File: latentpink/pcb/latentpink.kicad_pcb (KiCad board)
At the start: 8 copper layers, 145 x 134 mm, 244 parts, among them J1 CONN_SFP_HOST, J10 XILINX_JTAG, J13 CONN_01X05, J14 CONN_01X03, J2 SFP_CAGE, J3 RJ45, J4 RJ45, J5 BEL_FUSE_0826-1G1T-23-F, J6 BARREL_JACK, J7 RJ45, J8 08263-2X6R-54-F, J9 XILINX_JTAG, M1 960-27-12-D-AB-0, M2 960-23-23-F-AB-0, M3 SCREWHOLE, M4 SCREWHOLE, M5 SCREWHOLE, M6 SCREWHOLE, U1 VSC8512, U10 MYMGK1R812ERSR, U11 MYMGK00504ERSR, U12 STM32L031-QFN32, U13 MYMGK00504ERSR, U14 MYMGK00504ERSR, U15 MYMGK00504ERSR, U16 NCP45521IMNTWG-H, U17 NCP45521IMNTWG-H, U18 LP2996AMRE, U2 XC7K160T-2FBG484C, U3 CY7C2245KV18-450BZXI, U4 STM32H735-UFBGA176-25, U5 DP83867, U6 DP83867, U7 BEL_FUSE_S558-5999-M8-F, U8 BEL_FUSE_S558-5999-M8-F, U9 KSZ9031RN

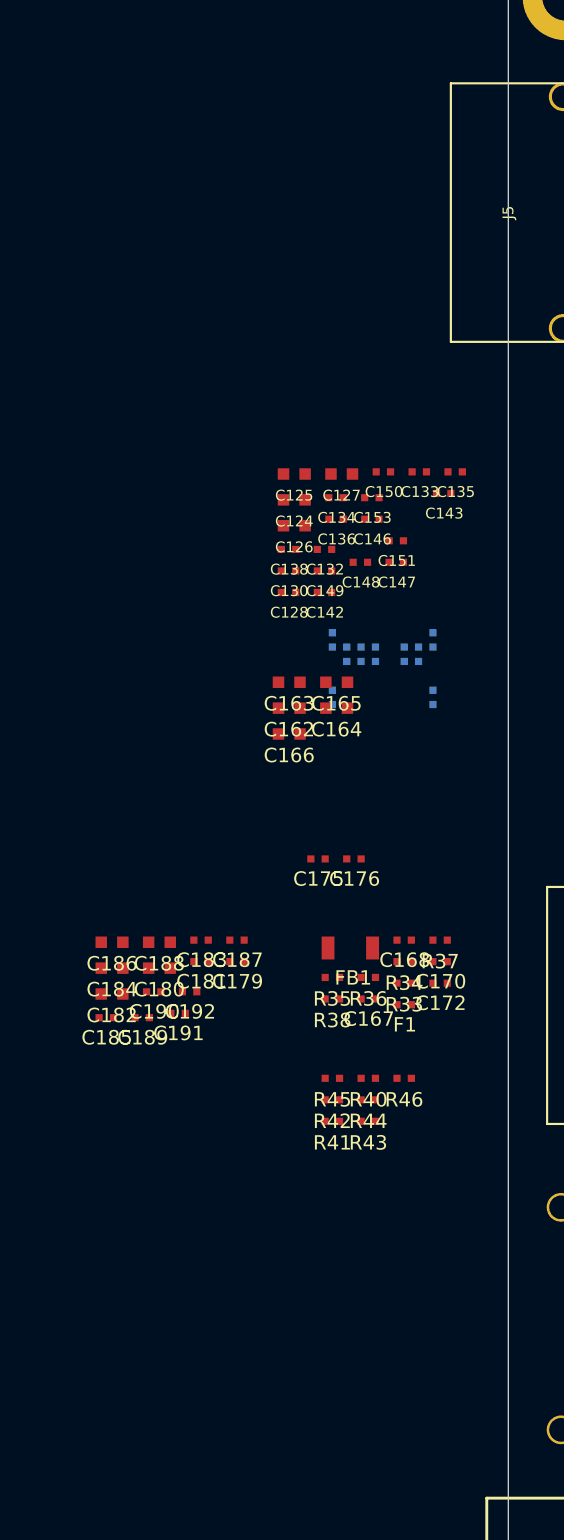
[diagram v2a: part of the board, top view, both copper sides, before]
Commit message: Initial version of RGMII PHY schematic
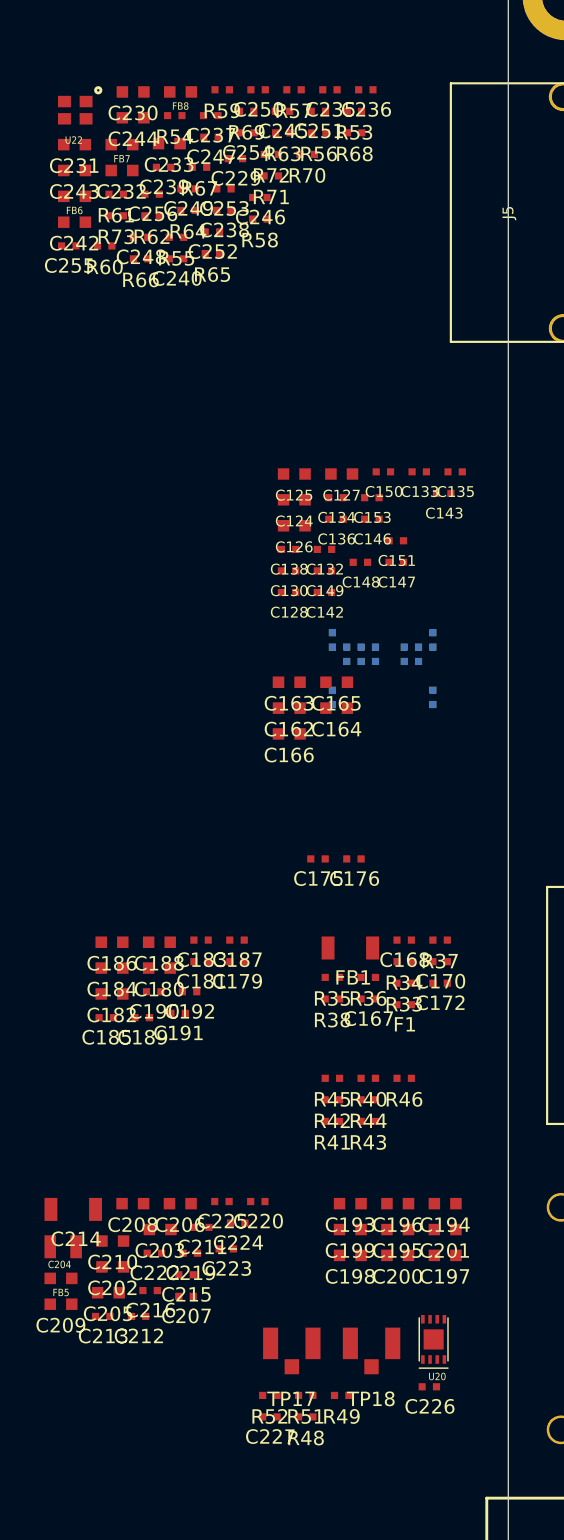
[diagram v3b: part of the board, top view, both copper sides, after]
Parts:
- added C193: 4.7 uF, azonenberg_pcb:EIA_0603_CAP_NOSILK, F.Cu at (26.0, 111.0)
- added C194: 4.7 uF, azonenberg_pcb:EIA_0603_CAP_NOSILK, F.Cu at (32.6, 111.0)
- added C195: 4.7 uF, azonenberg_pcb:EIA_0603_CAP_NOSILK, F.Cu at (29.3, 112.8)
- added C196: 4.7 uF, azonenberg_pcb:EIA_0603_CAP_NOSILK, F.Cu at (29.3, 111.0)
- added C197: 4.7 uF, azonenberg_pcb:EIA_0603_CAP_NOSILK, F.Cu at (32.6, 114.6)
- added C198: 4.7 uF, azonenberg_pcb:EIA_0603_CAP_NOSILK, F.Cu at (26.0, 114.6)
- added C199: 4.7 uF, azonenberg_pcb:EIA_0603_CAP_NOSILK, F.Cu at (26.0, 112.8)
- added C200: 4.7 uF, azonenberg_pcb:EIA_0603_CAP_NOSILK, F.Cu at (29.3, 114.6)
- added C201: 4.7 uF, azonenberg_pcb:EIA_0603_CAP_NOSILK, F.Cu at (32.6, 112.8)
- added C202: 4.7 uF, azonenberg_pcb:EIA_0603_CAP_NOSILK, F.Cu at (9.46, 115.4)
- added C203: 4.7 uF, azonenberg_pcb:EIA_0603_CAP_NOSILK, F.Cu at (12.8, 112.8)
- added C204: 10 uF, azonenberg_pcb:EIA_0805_CAP_NOSILK, F.Cu at (6.01, 114.0)
- added C205: 2.2 uF, azonenberg_pcb:EIA_0603_CAP_NOSILK, F.Cu at (9.16, 117.2)
- added C206: 4.7 uF, azonenberg_pcb:EIA_0603_CAP_NOSILK, F.Cu at (14.2, 111.0)
- added C207: 0.1 uF, azonenberg_pcb:EIA_0402_CAP_NOSILK, F.Cu at (14.6, 117.5)
- added C208: 4.7 uF, azonenberg_pcb:EIA_0603_CAP_NOSILK, F.Cu at (10.9, 111.0)
- added C209: 2.2 uF, azonenberg_pcb:EIA_0603_CAP_NOSILK, F.Cu at (5.86, 118.0)
- added C210: 4.7 uF, azonenberg_pcb:EIA_0603_CAP_NOSILK, F.Cu at (9.46, 113.6)
- added C211: 0.47 uF, azonenberg_pcb:EIA_0402_CAP_NOSILK, F.Cu at (15.7, 112.7)
- added C212: 0.47 uF, azonenberg_pcb:EIA_0402_CAP_NOSILK, F.Cu at (11.3, 118.8)
- added C213: 0.47 uF, azonenberg_pcb:EIA_0402_CAP_NOSILK, F.Cu at (8.76, 118.8)
- added C214: 22 uF, azonenberg_pcb:EIA_1206_CAP_NOSILK, F.Cu at (6.71, 111.4)
- added C215: 0.47 uF, azonenberg_pcb:EIA_0402_CAP_NOSILK, F.Cu at (14.6, 116.0)
- added C216: 0.47 uF, azonenberg_pcb:EIA_0402_CAP_NOSILK, F.Cu at (12.1, 117.0)
- added C219: 0.47 uF, azonenberg_pcb:EIA_0402_CAP_NOSILK, F.Cu at (14.9, 114.5)
- added C220: 0.47 uF, azonenberg_pcb:EIA_0402_CAP_NOSILK, F.Cu at (19.6, 110.8)
- added C222: 0.47 uF, azonenberg_pcb:EIA_0402_CAP_NOSILK, F.Cu at (12.4, 114.5)
- added C223: 0.47 uF, azonenberg_pcb:EIA_0402_CAP_NOSILK, F.Cu at (17.4, 114.2)
- added C224: 0.47 uF, azonenberg_pcb:EIA_0402_CAP_NOSILK, F.Cu at (18.2, 112.3)
- added C225: 0.47 uF, azonenberg_pcb:EIA_0402_CAP_NOSILK, F.Cu at (17.1, 110.8)
- added C226: 0.1 uF, azonenberg_pcb:EIA_0402_CAP_NOSILK, F.Cu at (31.5, 123.8)
- added C227: 0.47 uF, azonenberg_pcb:EIA_0402_CAP_NOSILK, F.Cu at (20.4, 125.8)
- added C229: 0.1 uF, azonenberg_pcb:EIA_0402_CAP_NOSILK, F.Cu at (18.0, 38.2)
- added C230: 4.7 uF, azonenberg_pcb:EIA_0603_CAP_NOSILK, F.Cu at (10.9, 33.6)
- added C231: 4.7 uF, azonenberg_pcb:EIA_0603_CAP_NOSILK, F.Cu at (6.80, 37.3)
- added C232: 4.7 uF, azonenberg_pcb:EIA_0603_CAP_NOSILK, F.Cu at (10.1, 39.1)
- added C233: 4.7 uF, azonenberg_pcb:EIA_0603_CAP_NOSILK, F.Cu at (13.4, 37.2)
- added C235: 0.1 uF, azonenberg_pcb:EIA_0402_CAP_NOSILK, F.Cu at (24.6, 33.5)
- added C236: 0.1 uF, azonenberg_pcb:EIA_0402_CAP_NOSILK, F.Cu at (27.1, 33.5)
- added C237: 0.1 uF, azonenberg_pcb:EIA_0402_CAP_NOSILK, F.Cu at (16.3, 35.2)
- added C238: 0.1 uF, azonenberg_pcb:EIA_0402_CAP_NOSILK, F.Cu at (17.2, 41.9)
- added C239: 0.47 uF, azonenberg_pcb:EIA_0402_CAP_NOSILK, F.Cu at (13.0, 38.9)
- added C240: 0.47 uF, azonenberg_pcb:EIA_0402_CAP_NOSILK, F.Cu at (13.9, 45.2)
- added C242: 4.7 uF, azonenberg_pcb:EIA_0603_CAP_NOSILK, F.Cu at (6.80, 42.7)
- added C243: 4.7 uF, azonenberg_pcb:EIA_0603_CAP_NOSILK, F.Cu at (6.80, 39.1)
- added C244: 4.7 uF, azonenberg_pcb:EIA_0603_CAP_NOSILK, F.Cu at (10.9, 35.4)
- added C245: 0.47 uF, azonenberg_pcb:EIA_0402_CAP_NOSILK, F.Cu at (21.3, 35.0)
- added C246: 0.47 uF, azonenberg_pcb:EIA_0402_CAP_NOSILK, F.Cu at (19.7, 41.0)
- added C247: 0.47 uF, azonenberg_pcb:EIA_0402_CAP_NOSILK, F.Cu at (16.3, 36.8)
- added C248: 0.47 uF, azonenberg_pcb:EIA_0402_CAP_NOSILK, F.Cu at (11.4, 43.7)
- added C249: 0.47 uF, azonenberg_pcb:EIA_0402_CAP_NOSILK, F.Cu at (14.7, 40.4)
- added C250: 0.47 uF, azonenberg_pcb:EIA_0402_CAP_NOSILK, F.Cu at (19.6, 33.5)
- added C251: 0.47 uF, azonenberg_pcb:EIA_0402_CAP_NOSILK, F.Cu at (23.8, 35.0)
- added C252: 0.47 uF, azonenberg_pcb:EIA_0402_CAP_NOSILK, F.Cu at (16.4, 43.4)
- added C253: 0.47 uF, azonenberg_pcb:EIA_0402_CAP_NOSILK, F.Cu at (17.2, 40.4)
- added C254: 0.47 uF, azonenberg_pcb:EIA_0402_CAP_NOSILK, F.Cu at (18.8, 36.5)
- added C255: 0.47 uF, azonenberg_pcb:EIA_0402_CAP_NOSILK, F.Cu at (6.40, 44.3)
- added C256: 0.47 uF, azonenberg_pcb:EIA_0402_CAP_NOSILK, F.Cu at (12.2, 40.7)
- added FB5: FERRITE_SMALL2, azonenberg_pcb:EIA_0603_INDUCTOR_NOSILK, F.Cu at (5.86, 116.2)
- added FB6: MI0603J601R-10, azonenberg_pcb:EIA_0603_INDUCTOR_NOSILK, F.Cu at (6.80, 40.9)
- added FB7: MI0603J601R-10, azonenberg_pcb:EIA_0603_INDUCTOR_NOSILK, F.Cu at (10.1, 37.3)
- added FB8: MI0603J601R-10, azonenberg_pcb:EIA_0603_INDUCTOR_NOSILK, F.Cu at (14.2, 33.6)
- added R48: 10K, azonenberg_pcb:EIA_0402_RES_NOSILK, F.Cu at (22.9, 125.8)
- added R49: 10K, azonenberg_pcb:EIA_0402_RES_NOSILK, F.Cu at (25.4, 124.3)
- added R51: 4.7K, azonenberg_pcb:EIA_0402_RES_NOSILK, F.Cu at (22.9, 124.3)
- added R52: 4.7K, azonenberg_pcb:EIA_0402_RES_NOSILK, F.Cu at (20.4, 124.3)
- added R53: 1M, azonenberg_pcb:EIA_0402_RES_NOSILK, F.Cu at (26.3, 35.0)
- added R54: 470, azonenberg_pcb:EIA_0402_RES_NOSILK, F.Cu at (13.8, 35.2)
- added R55: 470, azonenberg_pcb:EIA_0402_RES_NOSILK, F.Cu at (13.9, 43.7)
- added R56: 33, azonenberg_pcb:EIA_0402_RES_NOSILK, F.Cu at (23.8, 36.5)
- added R57: 1K, azonenberg_pcb:EIA_0402_RES_NOSILK, F.Cu at (22.1, 33.5)
- added R58: 33, azonenberg_pcb:EIA_0402_RES_NOSILK, F.Cu at (19.7, 42.5)
- added R59: 33, azonenberg_pcb:EIA_0402_RES_NOSILK, F.Cu at (17.1, 33.5)
- added R60: 33, azonenberg_pcb:EIA_0402_RES_NOSILK, F.Cu at (8.90, 44.3)
- added R61: 33, azonenberg_pcb:EIA_0402_RES_NOSILK, F.Cu at (9.70, 40.7)
- added R62: 33, azonenberg_pcb:EIA_0402_RES_NOSILK, F.Cu at (12.2, 42.2)
- added R63: 33, azonenberg_pcb:EIA_0402_RES_NOSILK, F.Cu at (21.3, 36.5)
- added R64: 12.1K 1%, azonenberg_pcb:EIA_0402_RES_NOSILK, F.Cu at (14.7, 41.9)
- added R65: 1K, azonenberg_pcb:EIA_0402_RES_NOSILK, F.Cu at (16.4, 44.9)
- added R66: 10K, azonenberg_pcb:EIA_0402_RES_NOSILK, F.Cu at (11.4, 45.2)
- added R67: 10K, azonenberg_pcb:EIA_0402_RES_NOSILK, F.Cu at (15.5, 38.9)
- added R68: 10K, azonenberg_pcb:EIA_0402_RES_NOSILK, F.Cu at (26.3, 36.5)
- added R69: 10K, azonenberg_pcb:EIA_0402_RES_NOSILK, F.Cu at (18.8, 35.0)
- added R70: 10K, azonenberg_pcb:EIA_0402_RES_NOSILK, F.Cu at (23.0, 38.0)
- added R71: 10K, azonenberg_pcb:EIA_0402_RES_NOSILK, F.Cu at (20.5, 39.5)
- added R72: 10K, azonenberg_pcb:EIA_0402_RES_NOSILK, F.Cu at (20.5, 38.0)
- added R73: 1K, azonenberg_pcb:EIA_0402_RES_NOSILK, F.Cu at (9.70, 42.2)
- added TP17: U.FL, azonenberg_pcb:CONN_U.FL_TE_1909763-1, F.Cu at (21.9, 120.8)
- added TP18: U.FL, azonenberg_pcb:CONN_U.FL_TE_1909763-1, F.Cu at (27.5, 120.8)
- added U20: AT24MAC402, azonenberg_pcb:DFN_8_0.5MM_2x3MM_TALL, F.Cu at (31.8, 120.5)
- added U22: ECS-2016MVQ-250-CN, azonenberg_pcb:OSCILLATOR_2.0x1.6, F.Cu at (6.85, 34.9)
- J5: value BEL_FUSE_0826-1G1T-23-F -> 0826-1G1T-23-F
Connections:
- J10 pad 10: unconnected-(J10-Pad10) -> /Management/MCU_JTAG_TDI
- J10 pad 11: unconnected-(J10-Pad11) -> /GND
- J10 pad 2: unconnected-(J10-Pad2) -> /3V3
- J10 pad 3: unconnected-(J10-Pad3) -> /GND
- J10 pad 4: unconnected-(J10-Pad4) -> /Management/MCU_JTAG_TMS
- J10 pad 5: unconnected-(J10-Pad5) -> /GND
- J10 pad 6: unconnected-(J10-Pad6) -> /Management/MCU_JTAG_TCK
- J10 pad 7: unconnected-(J10-Pad7) -> /GND
- J10 pad 8: unconnected-(J10-Pad8) -> /Management/MCU_JTAG_TDO
- J10 pad 9: unconnected-(J10-Pad9) -> /GND
- J5 pad 1: unconnected-(J5-Pad1) -> Net-(J5-Pad1)
- J5 pad 10: unconnected-(J5-Pad10) -> /Management/RGMII PHY/ETH_A_N
- J5 pad 11: unconnected-(J5-Pad11) -> /Management/RGMII PHY/ETH_A_P
- J5 pad 12: unconnected-(J5-Pad12) -> Net-(J5-Pad12)
- J5 pad 13: unconnected-(J5-Pad13) -> /GND
- J5 pad 14: unconnected-(J5-Pad14) -> Net-(J5-Pad14)
- J5 pad 15: unconnected-(J5-Pad15) -> /GND
- J5 pad 16: unconnected-(J5-Pad16) -> Net-(J5-Pad16)
- J5 pad 17: unconnected-(J5-Pad17) -> Net-(J5-Pad17)
- J5 pad 2: unconnected-(J5-Pad2) -> /Management/RGMII PHY/ETH_C_N
- J5 pad 3: unconnected-(J5-Pad3) -> /Management/RGMII PHY/ETH_C_P
- J5 pad 4: unconnected-(J5-Pad4) -> /Management/RGMII PHY/ETH_B_P
- J5 pad 5: unconnected-(J5-Pad5) -> /Management/RGMII PHY/ETH_B_N
- J5 pad 6: unconnected-(J5-Pad6) -> Net-(J5-Pad6)
- J5 pad 7: unconnected-(J5-Pad7) -> Net-(J5-Pad7)
- J5 pad 8: unconnected-(J5-Pad8) -> /Management/RGMII PHY/ETH_D_P
- J5 pad 9: unconnected-(J5-Pad9) -> /Management/RGMII PHY/ETH_D_N
- U12 pad 14: /Power Supply/MCU_RST_N -> /MCU_RST_N
- U12 pad 15: /Power Supply/FPGA_RST_N -> /FPGA/FPGA_RST_N
- U12 pad 16: /Power Supply/FPGA_DONE -> /FPGA/FPGA_DONE
- U12 pad 26: /Power Supply/FPGA_INIT -> /FPGA/FPGA_INIT
- U2 pad A10: unconnected-(U2-PadA10) -> /Management/MCU_QSPI_DQ3
- U2 pad A11: unconnected-(U2-PadA11) -> /Management/MCU_QSPI_DQ2
- U2 pad A8: unconnected-(U2-PadA8) -> /Management/MCU_QSPI_CLK
- U2 pad A9: unconnected-(U2-PadA9) -> /Management/MCU_IRQ
- U2 pad AA4: unconnected-(U2-PadAA4) -> /Management/RGMII PHY/ETH_LED1_N_1V8
- U2 pad AB3: unconnected-(U2-PadAB3) -> /Management/RGMII PHY/ETH_LED2_N_1V8
- U2 pad B8: unconnected-(U2-PadB8) -> /Management/MCU_QSPI_DQ1
- U2 pad C8: unconnected-(U2-PadC8) -> /Management/MCU_QSPI_DQ0
- U2 pad D10: unconnected-(U2-PadD10) -> /Management/ETH_LED2_P
- U2 pad E8: unconnected-(U2-PadE8) -> /Management/MCU_QSPI_CS_N
- U2 pad F14: unconnected-(U2-PadF14) -> /Management/ETH_LED1_P
- U2 pad F19: /FPGA/QDR SRAM/QDR_A1 -> /FPGA/QDR SRAM/FPGA_FLASH_DQ3
- U2 pad G18: /FPGA/QDR SRAM/QDR_A0 -> /FPGA/QDR SRAM/FPGA_FLASH_DQ2
- U2 pad H18: /FPGA/QDR SRAM/QDR_RPS_N -> /FPGA/QDR SRAM/FPGA_FLASH_DQ0
- U2 pad H19: /FPGA/QDR SRAM/QDR_QVLD -> /FPGA/QDR SRAM/FPGA_FLASH_DQ1
- U2 pad K18: /FPGA/QDR SRAM/QDR_A2 -> Net-(U2-PadK18)
- U2 pad K22: unconnected-(U2-PadK22) -> /FPGA/QDR SRAM/QDR_A8
- U2 pad K4: unconnected-(U2-PadK4) -> /Management/RGMII PHY/DCI_VRN_34
- U2 pad L16: /FPGA/QDR SRAM/QDR_A8 -> /FPGA/QDR SRAM/FPGA_FLASH_CS_N
- U2 pad L21: unconnected-(U2-PadL21) -> /FPGA/QDR SRAM/QDR_A1
- U2 pad L3: unconnected-(U2-PadL3) -> /Management/RGMII PHY/ETH_LED1_N_1V8
- U2 pad L4: unconnected-(U2-PadL4) -> /Management/RGMII PHY/RGMII_TXD3
- U2 pad L5: unconnected-(U2-PadL5) -> /Management/RGMII PHY/RGMII_TXD2
- U2 pad M20: unconnected-(U2-PadM20) -> /FPGA/QDR SRAM/QDR_A0
- U2 pad M21: unconnected-(U2-PadM21) -> /FPGA/QDR SRAM/QDR_QVLD
- U2 pad M3: unconnected-(U2-PadM3) -> /Management/RGMII PHY/ETH_LED2_N_1V8
- U2 pad M5: unconnected-(U2-PadM5) -> /Management/RGMII PHY/ETH_RST_N
- U2 pad N2: unconnected-(U2-PadN2) -> /Management/RGMII PHY/RGMII_TXD1
- U2 pad N20: unconnected-(U2-PadN20) -> /FPGA/QDR SRAM/QDR_RPS_N
- U2 pad N3: unconnected-(U2-PadN3) -> /Management/RGMII PHY/RGMII_TXD0
- U2 pad N4: unconnected-(U2-PadN4) -> /Management/RGMII PHY/ETH_RXD3
- U2 pad P1: unconnected-(U2-PadP1) -> /Management/RGMII PHY/ETH_MDC
- U2 pad P2: unconnected-(U2-PadP2) -> /Management/RGMII PHY/RGMII_TX_CLK
- U2 pad P4: unconnected-(U2-PadP4) -> /Management/RGMII PHY/ETH_RXD0
- U2 pad R1: unconnected-(U2-PadR1) -> /Management/RGMII PHY/ETH_MDIO
- U2 pad R18: unconnected-(U2-PadR18) -> /FPGA/QDR SRAM/QDR_A2
- U2 pad R2: unconnected-(U2-PadR2) -> /Management/RGMII PHY/RGMII_TX_EN
- U2 pad R3: unconnected-(U2-PadR3) -> /Management/RGMII PHY/CLK_125_P
- U2 pad R4: unconnected-(U2-PadR4) -> /Management/RGMII PHY/ETH_RX_DV
- U2 pad T1: unconnected-(U2-PadT1) -> /Management/RGMII PHY/ETH_RXD2
- U2 pad T3: unconnected-(U2-PadT3) -> /Management/RGMII PHY/CLK_125_N
- U2 pad T4: unconnected-(U2-PadT4) -> /Management/RGMII PHY/ETH_RX_CLK
- U2 pad U1: unconnected-(U2-PadU1) -> /Management/RGMII PHY/ETH_RXD1
- U2 pad V5: unconnected-(U2-PadV5) -> /Management/RGMII PHY/DCI_VRP_34
- U4 pad A11: unconnected-(U4-PadA11) -> /Management/MCU_JTAG_TDI
- U4 pad A12: unconnected-(U4-PadA12) -> /Management/MCU_JTAG_TCK
- U4 pad A13: unconnected-(U4-PadA13) -> /Management/MCU_VSMPS
- U4 pad A14: unconnected-(U4-PadA14) -> /Management/VCORE
- U4 pad A3: unconnected-(U4-PadA3) -> /Management/MCU_VSMPS
- U4 pad A4: unconnected-(U4-PadA4) -> /Management/VCORE
- U4 pad A6: unconnected-(U4-PadA6) -> Net-(U4-PadA6)
- U4 pad B13: unconnected-(U4-PadB13) -> /Management/MCU_JTAG_TMS
- U4 pad B15: unconnected-(U4-PadB15) -> /Management/MCU_UART_TX
- U4 pad C15: unconnected-(U4-PadC15) -> /Management/MCU_UART_RX
- U4 pad C5: unconnected-(U4-PadC5) -> /Management/MCU_BOOT0
- U4 pad D11: unconnected-(U4-PadD11) -> /3V3
- U4 pad D4: unconnected-(U4-PadD4) -> /3V3
- U4 pad D5: unconnected-(U4-PadD5) -> /3V3
- U4 pad E12: unconnected-(U4-PadE12) -> /3V3
- U4 pad E15: unconnected-(U4-PadE15) -> /3V3
- U4 pad E2: unconnected-(U4-PadE2) -> /3V3
- U4 pad E4: unconnected-(U4-PadE4) -> /3V3
- U4 pad F1: unconnected-(U4-PadF1) -> /Management/VLXSMPS
- U4 pad F13: unconnected-(U4-PadF13) -> /3V3
- U4 pad G1: unconnected-(U4-PadG1) -> /3V3
- U4 pad G2: unconnected-(U4-PadG2) -> /Management/VSMPS
- U4 pad G4: unconnected-(U4-PadG4) -> /3V3
- U4 pad H12: unconnected-(U4-PadH12) -> /3V3
- U4 pad K4: unconnected-(U4-PadK4) -> /3V3
- U4 pad L1: unconnected-(U4-PadL1) -> /MCU_RST_N
- U4 pad L12: unconnected-(U4-PadL12) -> /3V3
- U4 pad L4: unconnected-(U4-PadL4) -> /GND
- U4 pad M1: unconnected-(U4-PadM1) -> /Management/MCU_QSPI_DQ2
- U4 pad M3: unconnected-(U4-PadM3) -> /3V3
- U4 pad M4: unconnected-(U4-PadM4) -> /Management/MCU_VDDA
- U4 pad M5: unconnected-(U4-PadM5) -> /3V3
- U4 pad M9: unconnected-(U4-PadM9) -> /3V3
- U4 pad P1: unconnected-(U4-PadP1) -> /Management/MCU_IRQ
- U4 pad P2: unconnected-(U4-PadP2) -> /Management/MCU_QSPI_DQ3
- U4 pad P7: unconnected-(U4-PadP7) -> /Management/MCU_QSPI_CLK
- U4 pad R12: unconnected-(U4-PadR12) -> /Management/MCU_QSPI_CS_N
- U4 pad R13: unconnected-(U4-PadR13) -> /Management/VCORE
- U4 pad R14: unconnected-(U4-PadR14) -> /Management/MCU_VSMPS
- U4 pad R2: unconnected-(U4-PadR2) -> /Management/MCU_QSPI_DQ0
- U4 pad R8: unconnected-(U4-PadR8) -> /Management/MCU_QSPI_DQ1
- U9 pad 1: unconnected-(U9-Pad1) -> /Management/RGMII PHY/A2V5
- U9 pad 10: unconnected-(U9-Pad10) -> /Management/RGMII PHY/ETH_D_P
- U9 pad 11: unconnected-(U9-Pad11) -> /Management/RGMII PHY/ETH_D_N
- U9 pad 12: unconnected-(U9-Pad12) -> /Management/RGMII PHY/A2V5
- U9 pad 13: unconnected-(U9-Pad13) -> /GND
- U9 pad 14: unconnected-(U9-Pad14) -> /1V2
- U9 pad 15: unconnected-(U9-Pad15) -> /Management/RGMII PHY/ETH_LED2_N_1V8
- U9 pad 16: unconnected-(U9-Pad16) -> /1V8_IO
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
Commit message: Continued work on QSGMII subsystem
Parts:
- added C257: 0.47 uF, azonenberg_pcb:EIA_0402_CAP_NOSILK, F.Cu at (252.5, 59.8)
- added C258: 0.1 uF, azonenberg_pcb:EIA_0402_CAP_NOSILK, F.Cu at (104.5, 78.8)
- added C259: 0.1 uF, azonenberg_pcb:EIA_0402_CAP_NOSILK, F.Cu at (102.0, 80.2)
- added C260: 0.1 uF, azonenberg_pcb:EIA_0402_CAP_NOSILK, F.Cu at (102.0, 78.8)
- added C261: 0.1 uF, azonenberg_pcb:EIA_0402_CAP_NOSILK, F.Cu at (104.5, 80.2)
- added C264: 0.47 uF, azonenberg_pcb:EIA_0402_CAP_NOSILK, F.Cu at (228.0, 71.8)
- added C266: 0.47 uF, azonenberg_pcb:EIA_0402_CAP_NOSILK, F.Cu at (220.5, 69.7)
- added C267: 4.7 uF, azonenberg_pcb:EIA_0603_CAP_NOSILK, F.Cu at (220.9, 63.5)
- added C268: 0.47 uF, azonenberg_pcb:EIA_0402_CAP_NOSILK, F.Cu at (228.0, 68.8)
- added C269: 0.47 uF, azonenberg_pcb:EIA_0402_CAP_NOSILK, F.Cu at (234.6, 59.8)
- added C270: 0.47 uF, azonenberg_pcb:EIA_0402_CAP_NOSILK, F.Cu at (233.0, 67.2)
- added C271: 0.47 uF, azonenberg_pcb:EIA_0402_CAP_NOSILK, F.Cu at (239.6, 59.8)
- added C272: 0.47 uF, azonenberg_pcb:EIA_0402_CAP_NOSILK, F.Cu at (220.5, 66.7)
- added C273: 0.47 uF, azonenberg_pcb:EIA_0402_CAP_NOSILK, F.Cu at (236.3, 64.2)
- added C274: 0.47 uF, azonenberg_pcb:EIA_0402_CAP_NOSILK, F.Cu at (239.6, 61.2)
- added C275: 0.47 uF, azonenberg_pcb:EIA_0402_CAP_NOSILK, F.Cu at (233.8, 62.8)
- added C276: 0.47 uF, azonenberg_pcb:EIA_0402_CAP_NOSILK, F.Cu at (220.5, 68.2)
- added C277: 0.47 uF, azonenberg_pcb:EIA_0402_CAP_NOSILK, F.Cu at (230.5, 71.8)
- added C278: 0.47 uF, azonenberg_pcb:EIA_0402_CAP_NOSILK, F.Cu at (228.8, 64.2)
- added C279: 0.47 uF, azonenberg_pcb:EIA_0402_CAP_NOSILK, F.Cu at (242.1, 59.8)
- added C280: 0.47 uF, azonenberg_pcb:EIA_0402_CAP_NOSILK, F.Cu at (223.0, 66.7)
- added C281: 0.47 uF, azonenberg_pcb:EIA_0402_CAP_NOSILK, F.Cu at (228.8, 62.8)
- added C282: 0.47 uF, azonenberg_pcb:EIA_0402_CAP_NOSILK, F.Cu at (223.0, 71.2)
- added C285: 0.47 uF, azonenberg_pcb:EIA_0402_CAP_NOSILK, F.Cu at (228.0, 65.8)
- added C286: 0.47 uF, azonenberg_pcb:EIA_0402_CAP_NOSILK, F.Cu at (230.5, 68.8)
- added C287: 0.47 uF, azonenberg_pcb:EIA_0402_CAP_NOSILK, F.Cu at (235.5, 67.2)
- added C288: 0.47 uF, azonenberg_pcb:EIA_0402_CAP_NOSILK, F.Cu at (230.5, 65.8)
- added C290: 0.47 uF, azonenberg_pcb:EIA_0402_CAP_NOSILK, F.Cu at (242.1, 61.2)
- added C291: 0.47 uF, azonenberg_pcb:EIA_0402_CAP_NOSILK, F.Cu at (233.8, 64.2)
- added C292: 4.7 uF, azonenberg_pcb:EIA_0603_CAP_NOSILK, F.Cu at (224.2, 59.9)
- added C293: 4.7 uF, azonenberg_pcb:EIA_0603_CAP_NOSILK, F.Cu at (220.9, 61.7)
- added C294: 0.47 uF, azonenberg_pcb:EIA_0402_CAP_NOSILK, F.Cu at (233.0, 68.8)
- added C295: 0.47 uF, azonenberg_pcb:EIA_0402_CAP_NOSILK, F.Cu at (234.6, 61.2)
- added C296: 0.47 uF, azonenberg_pcb:EIA_0402_CAP_NOSILK, F.Cu at (223.8, 63.4)
- added C297: 0.47 uF, azonenberg_pcb:EIA_0402_CAP_NOSILK, F.Cu at (225.5, 70.8)
- added C298: 0.47 uF, azonenberg_pcb:EIA_0402_CAP_NOSILK, F.Cu at (233.0, 65.8)
- added C299: 0.47 uF, azonenberg_pcb:EIA_0402_CAP_NOSILK, F.Cu at (232.1, 59.8)
- added C300: 0.47 uF, azonenberg_pcb:EIA_0402_CAP_NOSILK, F.Cu at (225.5, 67.8)
- added C302: 0.47 uF, azonenberg_pcb:EIA_0402_CAP_NOSILK, F.Cu at (238.8, 62.8)
- added C303: 0.47 uF, azonenberg_pcb:EIA_0402_CAP_NOSILK, F.Cu at (225.5, 72.3)
- added C304: 0.47 uF, azonenberg_pcb:EIA_0402_CAP_NOSILK, F.Cu at (232.1, 61.2)
- added C305: 0.47 uF, azonenberg_pcb:EIA_0402_CAP_NOSILK, F.Cu at (227.1, 61.2)
- added C306: 4.7 uF, azonenberg_pcb:EIA_0603_CAP_NOSILK, F.Cu at (224.2, 61.7)
- added C307: 0.47 uF, azonenberg_pcb:EIA_0402_CAP_NOSILK, F.Cu at (220.5, 71.2)
- added C308: 0.47 uF, azonenberg_pcb:EIA_0402_CAP_NOSILK, F.Cu at (228.0, 70.2)
- added C309: 0.47 uF, azonenberg_pcb:EIA_0402_CAP_NOSILK, F.Cu at (228.0, 67.2)
- added C310: 0.47 uF, azonenberg_pcb:EIA_0402_CAP_NOSILK, F.Cu at (220.5, 65.2)
- added C311: 4.7 uF, azonenberg_pcb:EIA_0603_CAP_NOSILK, F.Cu at (220.9, 59.9)
- added C312: 0.47 uF, azonenberg_pcb:EIA_0402_CAP_NOSILK, F.Cu at (225.5, 69.3)
- added C313: 0.47 uF, azonenberg_pcb:EIA_0402_CAP_NOSILK, F.Cu at (237.1, 59.8)
- added C314: 0.47 uF, azonenberg_pcb:EIA_0402_CAP_NOSILK, F.Cu at (226.3, 63.4)
- added C315: 0.47 uF, azonenberg_pcb:EIA_0402_CAP_NOSILK, F.Cu at (237.1, 61.2)
- added C316: 0.47 uF, azonenberg_pcb:EIA_0402_CAP_NOSILK, F.Cu at (229.6, 59.8)
- added C317: 0.47 uF, azonenberg_pcb:EIA_0402_CAP_NOSILK, F.Cu at (223.0, 68.2)
- added C318: 0.47 uF, azonenberg_pcb:EIA_0402_CAP_NOSILK, F.Cu at (230.5, 67.2)
- added C319: 0.47 uF, azonenberg_pcb:EIA_0402_CAP_NOSILK, F.Cu at (231.3, 62.8)
- added C320: 0.47 uF, azonenberg_pcb:EIA_0402_CAP_NOSILK, F.Cu at (225.5, 64.8)
- added C321: 0.47 uF, azonenberg_pcb:EIA_0402_CAP_NOSILK, F.Cu at (223.0, 69.7)
- added C322: 0.47 uF, azonenberg_pcb:EIA_0402_CAP_NOSILK, F.Cu at (229.6, 61.2)
- added C323: 0.47 uF, azonenberg_pcb:EIA_0402_CAP_NOSILK, F.Cu at (223.0, 65.2)
- added C324: 0.47 uF, azonenberg_pcb:EIA_0402_CAP_NOSILK, F.Cu at (227.1, 59.8)
- added C325: 0.47 uF, azonenberg_pcb:EIA_0402_CAP_NOSILK, F.Cu at (236.3, 62.8)
- added C326: 0.47 uF, azonenberg_pcb:EIA_0402_CAP_NOSILK, F.Cu at (235.5, 65.8)
- added C327: 0.47 uF, azonenberg_pcb:EIA_0402_CAP_NOSILK, F.Cu at (235.5, 68.8)
- added C328: 0.47 uF, azonenberg_pcb:EIA_0402_CAP_NOSILK, F.Cu at (238.8, 64.2)
- added C329: 0.47 uF, azonenberg_pcb:EIA_0402_CAP_NOSILK, F.Cu at (231.3, 64.2)
- added C330: 0.47 uF, azonenberg_pcb:EIA_0402_CAP_NOSILK, F.Cu at (241.3, 62.8)
- added C331: 0.47 uF, azonenberg_pcb:EIA_0402_CAP_NOSILK, F.Cu at (225.5, 66.3)
- added C332: 0.47 uF, azonenberg_pcb:EIA_0402_CAP_NOSILK, F.Cu at (233.0, 70.2)
- added C333: 0.47 uF, azonenberg_pcb:EIA_0402_CAP_NOSILK, F.Cu at (230.5, 70.2)
- added C334: 0.1 uF, azonenberg_pcb:EIA_0402_CAP_NOSILK, F.Cu at (99.2, 69.8)
- added C335: 0.1 uF, azonenberg_pcb:EIA_0402_CAP_NOSILK, F.Cu at (101.8, 71.2)
- added C336: 0.1 uF, azonenberg_pcb:EIA_0402_CAP_NOSILK, F.Cu at (101.8, 72.8)
- added C337: 0.1 uF, azonenberg_pcb:EIA_0402_CAP_NOSILK, F.Cu at (101.8, 69.8)
- added C338: 0.1 uF, azonenberg_pcb:EIA_0402_CAP_NOSILK, F.Cu at (104.2, 71.2)
- added C339: 0.1 uF, azonenberg_pcb:EIA_0402_CAP_NOSILK, F.Cu at (101.8, 74.2)
- added C340: 0.1 uF, azonenberg_pcb:EIA_0402_CAP_NOSILK, F.Cu at (104.2, 72.8)
- added C341: 0.1 uF, azonenberg_pcb:EIA_0402_CAP_NOSILK, F.Cu at (99.2, 71.2)
- added C342: 0.1 uF, azonenberg_pcb:EIA_0402_CAP_NOSILK, F.Cu at (104.2, 69.8)
- added C343: 0.1 uF, azonenberg_pcb:EIA_0402_CAP_NOSILK, F.Cu at (99.2, 72.8)
- added C344: 0.47 uF, azonenberg_pcb:EIA_0402_CAP_NOSILK, F.Cu at (99.2, 74.2)
- added C345: 0.47 uF, azonenberg_pcb:EIA_0402_CAP_NOSILK, F.Cu at (106.8, 69.8)
- added C346: 0.1 uF, azonenberg_pcb:EIA_0402_CAP_NOSILK, F.Cu at (102.8, 66.5)
- added C347: 0.1 uF, azonenberg_pcb:EIA_0402_CAP_NOSILK, F.Cu at (102.8, 65.0)
- added C348: 0.1 uF, azonenberg_pcb:EIA_0402_CAP_NOSILK, F.Cu at (105.2, 66.5)
- added C349: 0.1 uF, azonenberg_pcb:EIA_0402_CAP_NOSILK, F.Cu at (105.2, 65.0)
- added C350: 0.1 uF, azonenberg_pcb:EIA_0402_CAP_NOSILK, F.Cu at (100.2, 65.0)
- added C351: 0.1 uF, azonenberg_pcb:EIA_0402_CAP_NOSILK, F.Cu at (100.2, 66.5)
- added J16: JUMPER_0402_SPDT, azonenberg_pcb:EIA_0402_JUMPER, F.Cu at (249.5, 61.2)
- added J17: JUMPER_0402_SPDT, azonenberg_pcb:EIA_0402_JUMPER, F.Cu at (249.5, 59.8)
- added L2: HI1206N101R-10, azonenberg_pcb:EIA_1206_CAP_NOSILK, F.Cu at (13.2, 140.5)
- added L3: HI1206N101R-10, azonenberg_pcb:EIA_1206_CAP_NOSILK, F.Cu at (18.2, 140.5)
- added L4: HI1206N101R-10, azonenberg_pcb:EIA_1206_CAP_NOSILK, F.Cu at (13.2, 137.9)
- added L5: HI1206N101R-10, azonenberg_pcb:EIA_1206_CAP_NOSILK, F.Cu at (18.2, 137.9)
- added R28: 470 1/4W, azonenberg_pcb:EIA_0603_RES_NOSILK, F.Cu at (30.3, 137.5)
- added R50: 33, azonenberg_pcb:EIA_0402_RES_NOSILK, F.Cu at (30.3, 145.2)
- added R74: 49.9, azonenberg_pcb:EIA_0402_RES_NOSILK, F.Cu at (16.6, 146.8)
- added R75: 49.9, azonenberg_pcb:EIA_0402_RES_NOSILK, F.Cu at (16.6, 148.3)
- added R76: 0, azonenberg_pcb:EIA_0402_RES_NOSILK, F.Cu at (23.6, 146.8)
- added R77: 10K, azonenberg_pcb:EIA_0402_RES_NOSILK, F.Cu at (12.8, 129.2)
- added R78: 4.7K, azonenberg_pcb:EIA_0402_RES_NOSILK, F.Cu at (14.0, 105.0)
- added R79: 4.7K, azonenberg_pcb:EIA_0402_RES_NOSILK, F.Cu at (16.5, 105.0)
- added U19: TPS7A2533DRVR, azonenberg_pcb:DFN_6_0.65MM_2x2MM, F.Cu at (27.0, 138.7)
- added U21: ECX2-LMV-3CN-125.000-TR, azonenberg_pcb:OSCILLATOR_LVDS_3.2x2.5, F.Cu at (13.1, 148.4)
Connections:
- C10 pad 1: /QSGMII PHY/QSGMII Power/1V0 -> /1V0
- C10 pad 2: /QSGMII PHY/QSGMII Power/GND -> /GND
- C11 pad 1: /QSGMII PHY/QSGMII Power/1V0 -> /1V0
- C11 pad 2: /QSGMII PHY/QSGMII Power/GND -> /GND
- C12 pad 1: /QSGMII PHY/QSGMII Power/1V0 -> /1V0
- C12 pad 2: /QSGMII PHY/QSGMII Power/GND -> /GND
- C13 pad 2: /QSGMII PHY/QSGMII Power/GND -> /GND
- C14 pad 2: /QSGMII PHY/QSGMII Power/GND -> /GND
- C15 pad 1: /QSGMII PHY/QSGMII Power/1V0 -> /1V0
- C15 pad 2: /QSGMII PHY/QSGMII Power/GND -> /GND
- C16 pad 1: /QSGMII PHY/QSGMII Power/1V0 -> /1V0
- C16 pad 2: /QSGMII PHY/QSGMII Power/GND -> /GND
- C17 pad 1: /QSGMII PHY/QSGMII Power/1V0 -> /1V0
- C17 pad 2: /QSGMII PHY/QSGMII Power/GND -> /GND
- C18 pad 1: /QSGMII PHY/QSGMII Power/1V0 -> /1V0
- C18 pad 2: /QSGMII PHY/QSGMII Power/GND -> /GND
- C19 pad 1: /QSGMII PHY/QSGMII Power/1V0 -> /1V0
- C19 pad 2: /QSGMII PHY/QSGMII Power/GND -> /GND
- C2 pad 1: /QSGMII PHY/QSGMII Power/1V0 -> /1V0
- C2 pad 2: /QSGMII PHY/QSGMII Power/GND -> /GND
- C20 pad 2: /QSGMII PHY/QSGMII Power/GND -> /GND
- C21 pad 2: /QSGMII PHY/QSGMII Power/GND -> /GND
- C22 pad 1: /QSGMII PHY/QSGMII Power/1V0 -> /1V0
- C22 pad 2: /QSGMII PHY/QSGMII Power/GND -> /GND
- C23 pad 1: /QSGMII PHY/QSGMII Power/1V0 -> /1V0
- C23 pad 2: /QSGMII PHY/QSGMII Power/GND -> /GND
- C24 pad 1: /QSGMII PHY/QSGMII Power/1V0 -> /1V0
- C24 pad 2: /QSGMII PHY/QSGMII Power/GND -> /GND
- C25 pad 1: /QSGMII PHY/QSGMII Power/1V0 -> /1V0
- C25 pad 2: /QSGMII PHY/QSGMII Power/GND -> /GND
- C26 pad 1: /QSGMII PHY/QSGMII Power/1V0 -> /1V0
- C26 pad 2: /QSGMII PHY/QSGMII Power/GND -> /GND
- C27 pad 2: /QSGMII PHY/QSGMII Power/GND -> /GND
- C28 pad 2: /QSGMII PHY/QSGMII Power/GND -> /GND
- C29 pad 1: /QSGMII PHY/QSGMII Power/1V0 -> /1V0
- C29 pad 2: /QSGMII PHY/QSGMII Power/GND -> /GND
- C3 pad 1: /QSGMII PHY/QSGMII Power/1V0 -> /1V0
- C3 pad 2: /QSGMII PHY/QSGMII Power/GND -> /GND
- C30 pad 1: /QSGMII PHY/QSGMII Power/1V0 -> /1V0
- C30 pad 2: /QSGMII PHY/QSGMII Power/GND -> /GND
- C31 pad 1: /QSGMII PHY/QSGMII Power/1V0 -> /1V0
- C31 pad 2: /QSGMII PHY/QSGMII Power/GND -> /GND
- C32 pad 1: /QSGMII PHY/QSGMII Power/1V0 -> /1V0
- C32 pad 2: /QSGMII PHY/QSGMII Power/GND -> /GND
- C33 pad 1: /QSGMII PHY/QSGMII Power/1V0 -> /1V0
- C33 pad 2: /QSGMII PHY/QSGMII Power/GND -> /GND
- C34 pad 2: /QSGMII PHY/QSGMII Power/GND -> /GND
- C35 pad 2: /QSGMII PHY/QSGMII Power/GND -> /GND
- C36 pad 1: /QSGMII PHY/QSGMII Power/1V0 -> /1V0
- C36 pad 2: /QSGMII PHY/QSGMII Power/GND -> /GND
- C37 pad 1: /QSGMII PHY/QSGMII Power/1V0 -> /1V0
- C37 pad 2: /QSGMII PHY/QSGMII Power/GND -> /GND
- C38 pad 1: /QSGMII PHY/QSGMII Power/1V0 -> /1V0
- C38 pad 2: /QSGMII PHY/QSGMII Power/GND -> /GND
- C39 pad 1: /QSGMII PHY/QSGMII Power/1V0 -> /1V0
- C39 pad 2: /QSGMII PHY/QSGMII Power/GND -> /GND
- C4 pad 1: /QSGMII PHY/QSGMII Power/1V0 -> /1V0
- C4 pad 2: /QSGMII PHY/QSGMII Power/GND -> /GND
- C40 pad 1: /QSGMII PHY/QSGMII Power/1V0 -> /1V0
- C40 pad 2: /QSGMII PHY/QSGMII Power/GND -> /GND
- C41 pad 2: /QSGMII PHY/QSGMII Power/GND -> /GND
- C42 pad 2: /QSGMII PHY/QSGMII Power/GND -> /GND
- C43 pad 1: /QSGMII PHY/QSGMII Power/1V0 -> /1V0
- C43 pad 2: /QSGMII PHY/QSGMII Power/GND -> /GND
- C44 pad 1: /QSGMII PHY/QSGMII Power/1V0 -> /1V0
- C44 pad 2: /QSGMII PHY/QSGMII Power/GND -> /GND
- C45 pad 1: /QSGMII PHY/QSGMII Power/1V0 -> /1V0
- C45 pad 2: /QSGMII PHY/QSGMII Power/GND -> /GND
- C46 pad 1: /QSGMII PHY/QSGMII Power/1V0 -> /1V0
- C46 pad 2: /QSGMII PHY/QSGMII Power/GND -> /GND
- C47 pad 1: /QSGMII PHY/QSGMII Power/1V0 -> /1V0
- C47 pad 2: /QSGMII PHY/QSGMII Power/GND -> /GND
- C48 pad 2: /QSGMII PHY/QSGMII Power/GND -> /GND
- C49 pad 2: /QSGMII PHY/QSGMII Power/GND -> /GND
- C5 pad 1: /QSGMII PHY/QSGMII Power/1V0 -> /1V0
- C5 pad 2: /QSGMII PHY/QSGMII Power/GND -> /GND
- C50 pad 1: /QSGMII PHY/QSGMII Power/1V0 -> /1V0
- C50 pad 2: /QSGMII PHY/QSGMII Power/GND -> /GND
- C51 pad 1: /QSGMII PHY/QSGMII Power/1V0 -> /1V0
- C51 pad 2: /QSGMII PHY/QSGMII Power/GND -> /GND
- C52 pad 1: /QSGMII PHY/QSGMII Power/1V0 -> /1V0
- C52 pad 2: /QSGMII PHY/QSGMII Power/GND -> /GND
- C53 pad 1: /QSGMII PHY/QSGMII Power/1V0 -> /1V0
- C53 pad 2: /QSGMII PHY/QSGMII Power/GND -> /GND
- C54 pad 2: /QSGMII PHY/QSGMII Power/GND -> /GND
- C55 pad 2: /QSGMII PHY/QSGMII Power/GND -> /GND
- C56 pad 1: /QSGMII PHY/QSGMII Power/1V0 -> /1V0
- C56 pad 2: /QSGMII PHY/QSGMII Power/GND -> /GND
- C57 pad 1: /QSGMII PHY/QSGMII Power/1V0 -> /1V0
- C57 pad 2: /QSGMII PHY/QSGMII Power/GND -> /GND
- C58 pad 1: /QSGMII PHY/QSGMII Power/1V0 -> /1V0
- C58 pad 2: /QSGMII PHY/QSGMII Power/GND -> /GND
- C59 pad 1: /QSGMII PHY/QSGMII Power/1V0 -> /1V0
- C59 pad 2: /QSGMII PHY/QSGMII Power/GND -> /GND
- C60 pad 2: /QSGMII PHY/QSGMII Power/GND -> /GND
- C61 pad 2: /QSGMII PHY/QSGMII Power/GND -> /GND
- C62 pad 1: /QSGMII PHY/QSGMII Power/1V0 -> /1V0
- C62 pad 2: /QSGMII PHY/QSGMII Power/GND -> /GND
- C63 pad 1: /QSGMII PHY/QSGMII Power/1V0 -> /1V0
- C63 pad 2: /QSGMII PHY/QSGMII Power/GND -> /GND
- C64 pad 1: /QSGMII PHY/QSGMII Power/1V0 -> /1V0
- C64 pad 2: /QSGMII PHY/QSGMII Power/GND -> /GND
- C65 pad 1: /QSGMII PHY/QSGMII Power/1V0 -> /1V0
- C65 pad 2: /QSGMII PHY/QSGMII Power/GND -> /GND
- C66 pad 2: /QSGMII PHY/QSGMII Power/GND -> /GND
- C68 pad 2: /QSGMII PHY/QSGMII Power/GND -> /GND
- C69 pad 2: /QSGMII PHY/QSGMII Power/GND -> /GND
- C7 pad 2: /QSGMII PHY/QSGMII Power/GND -> /GND
- C70 pad 2: /QSGMII PHY/QSGMII Power/GND -> /GND
- C71 pad 2: /QSGMII PHY/QSGMII Power/GND -> /GND
- C72 pad 2: /QSGMII PHY/QSGMII Power/GND -> /GND
- C73 pad 2: /QSGMII PHY/QSGMII Power/GND -> /GND
- C74 pad 2: /QSGMII PHY/QSGMII Power/GND -> /GND
- C75 pad 2: /QSGMII PHY/QSGMII Power/GND -> /GND
- C76 pad 2: /QSGMII PHY/QSGMII Power/GND -> /GND
- C77 pad 2: /QSGMII PHY/QSGMII Power/GND -> /GND
- C78 pad 2: /QSGMII PHY/QSGMII Power/GND -> /GND
- C79 pad 2: /QSGMII PHY/QSGMII Power/GND -> /GND
- C8 pad 1: /QSGMII PHY/QSGMII Power/1V0 -> /1V0
- C8 pad 2: /QSGMII PHY/QSGMII Power/GND -> /GND
- C80 pad 2: /QSGMII PHY/QSGMII Power/GND -> /GND
- C81 pad 2: /QSGMII PHY/QSGMII Power/GND -> /GND
- C82 pad 2: /QSGMII PHY/QSGMII Power/GND -> /GND
- C83 pad 2: /QSGMII PHY/QSGMII Power/GND -> /GND
- C84 pad 2: /QSGMII PHY/QSGMII Power/GND -> /GND
- C85 pad 2: /QSGMII PHY/QSGMII Power/GND -> /GND
- C86 pad 2: /QSGMII PHY/QSGMII Power/GND -> /GND
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
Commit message: Switched to new RJ45 for LATENTPINK, continued general PHY schematic
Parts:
- removed U7, U8: BEL_FUSE_S558-5999-M8-F, azonenberg_pcb:BELFUSE_S558-5999-M8-F
- added J15: CONN_01X03, azonenberg_pcb:CONN_HEADER_2.54MM_1x3, F.Cu at (268.5, 157.7)
- added J18: BEL_FUSE_0845-2R1T-E4, azonenberg_pcb:CONN_RJ45_BELFUSE_0845-2R1T-E4, F.Cu at (174.0, 90.5)
- added J19: BEL_FUSE_0845-2R1T-E4, azonenberg_pcb:CONN_RJ45_BELFUSE_0845-2R1T-E4, F.Cu at (174.0, 71.0)
- added J20: BEL_FUSE_0845-2R1T-E4, azonenberg_pcb:CONN_RJ45_BELFUSE_0845-2R1T-E4, F.Cu at (174.0, 51.5)
- added J21: BEL_FUSE_0845-2R1T-E4, azonenberg_pcb:CONN_RJ45_BELFUSE_0845-2R1T-E4, F.Cu at (174.0, 32.0)
- added J22: BEL_FUSE_0845-2R1T-E4, azonenberg_pcb:CONN_RJ45_BELFUSE_0845-2R1T-E4, F.Cu at (174.0, 149.0)
- added R100: 470, azonenberg_pcb:EIA_0402_RES_NOSILK, F.Cu at (133.0, 38.8)
- added R101: 470, azonenberg_pcb:EIA_0402_RES_NOSILK, F.Cu at (138.0, 43.2)
- added R102: 470, azonenberg_pcb:EIA_0402_RES_NOSILK, F.Cu at (130.5, 44.8)
- added R103: 470, azonenberg_pcb:EIA_0402_RES_NOSILK, F.Cu at (138.0, 40.2)
- added R104: 470, azonenberg_pcb:EIA_0402_RES_NOSILK, F.Cu at (133.0, 41.8)
- added R106: 1K, azonenberg_pcb:EIA_0402_RES_NOSILK, F.Cu at (133.8, 49.0)
- added R107: 1K, azonenberg_pcb:EIA_0402_RES_NOSILK, F.Cu at (136.2, 49.0)
- added R80: 100, azonenberg_pcb:EIA_0402_RES_NOSILK, F.Cu at (133.0, 44.8)
- added R81: 470, azonenberg_pcb:EIA_0402_RES_NOSILK, F.Cu at (138.0, 41.8)
- added R82: 470, azonenberg_pcb:EIA_0402_RES_NOSILK, F.Cu at (130.5, 38.8)
- added R83: 470, azonenberg_pcb:EIA_0402_RES_NOSILK, F.Cu at (138.0, 44.8)
- added R84: 470, azonenberg_pcb:EIA_0402_RES_NOSILK, F.Cu at (135.5, 44.8)
- added R85: 470, azonenberg_pcb:EIA_0402_RES_NOSILK, F.Cu at (138.0, 38.8)
- added R86: 470, azonenberg_pcb:EIA_0402_RES_NOSILK, F.Cu at (135.5, 43.2)
- added R87: 470, azonenberg_pcb:EIA_0402_RES_NOSILK, F.Cu at (143.0, 38.8)
- added R88: 470, azonenberg_pcb:EIA_0402_RES_NOSILK, F.Cu at (133.0, 43.2)
- added R89: 470, azonenberg_pcb:EIA_0402_RES_NOSILK, F.Cu at (133.0, 40.2)
- added R90: 470, azonenberg_pcb:EIA_0402_RES_NOSILK, F.Cu at (143.0, 40.2)
- added R91: 470, azonenberg_pcb:EIA_0402_RES_NOSILK, F.Cu at (140.5, 40.2)
- added R92: 470, azonenberg_pcb:EIA_0402_RES_NOSILK, F.Cu at (130.5, 43.2)
- added R93: 470, azonenberg_pcb:EIA_0402_RES_NOSILK, F.Cu at (140.5, 41.8)
- added R94: 470, azonenberg_pcb:EIA_0402_RES_NOSILK, F.Cu at (135.5, 38.8)
- added R95: 470, azonenberg_pcb:EIA_0402_RES_NOSILK, F.Cu at (130.5, 40.2)
- added R96: 470, azonenberg_pcb:EIA_0402_RES_NOSILK, F.Cu at (130.5, 41.8)
- added R97: 470, azonenberg_pcb:EIA_0402_RES_NOSILK, F.Cu at (135.5, 41.8)
- added R98: 470, azonenberg_pcb:EIA_0402_RES_NOSILK, F.Cu at (135.5, 40.2)
- added R99: 470, azonenberg_pcb:EIA_0402_RES_NOSILK, F.Cu at (140.5, 38.8)
- J3: value RJ45 -> XILINX_JTAG; footprint azonenberg_pcb:CONN_RJ45_BELSTEWART_SS-7188S-A-PG4-1-BA-xx -> azonenberg_pcb:XILINX_JTAG_PTH_MOLEX_0878311420
- J4: value RJ45 -> BEL_FUSE_0845-2R1T-E4; footprint azonenberg_pcb:CONN_RJ45_BELSTEWART_SS-7188S-A-PG4-1-BA-xx -> azonenberg_pcb:CONN_RJ45_BELFUSE_0845-2R1T-E4
- J8: value 08263-2X6R-54-F -> BEL_FUSE_0845-2R1T-E4; footprint azonenberg_pcb:CONN_RJ45_BELFUSE_0863-2X6R-54-F -> azonenberg_pcb:CONN_RJ45_BELFUSE_0845-2R1T-E4
- moved J3 130.6 mm to (128.0, 29.0)
- moved M3 16.6 mm to (141.0, 154.0)
- moved M6 5.00 mm to (47.0, 154.0)
- moved J8 2.71 mm to (174.0, 110.0)
- moved J4 2.14 mm to (174.0, 129.5)
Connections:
- J3 pad 2: unconnected-(J3-Pad2) -> /2V5
- J3 pad 3: unconnected-(J3-Pad3) -> /GND
- J3 pad 4: unconnected-(J3-Pad4) -> /QSGMII PHY/VSC_JTAG_TMS
- J3 pad 5: unconnected-(J3-Pad5) -> /GND
- J3 pad 6: unconnected-(J3-Pad6) -> /QSGMII PHY/VSC_JTAG_TCK
- J3 pad 7: unconnected-(J3-Pad7) -> /GND
- J3 pad 8: unconnected-(J3-Pad8) -> /QSGMII PHY/VSC_JTAG_TDO
- J3 pad 9: unconnected-(J3-Pad9) -> /GND
- J4 pad 1: unconnected-(J4-Pad1) -> /GND
- J4 pad 2: unconnected-(J4-Pad2) -> /QSGMII PHY/ETH0_D3_N
- J4 pad 3: unconnected-(J4-Pad3) -> /QSGMII PHY/ETH0_D2_P
- J4 pad 5: unconnected-(J4-Pad5) -> /QSGMII PHY/ETH0_D1_N
- J4 pad 6: unconnected-(J4-Pad6) -> /QSGMII PHY/ETH0_D0_P
- J4 pad 9: unconnected-(J4-Pad9) -> /QSGMII PHY/ETH0_D3_P
- R78 pad 2: /QSGMII PHY/3V3 -> /3V3
- R79 pad 2: /QSGMII PHY/3V3 -> /3V3
- U1 pad AA1: unconnected-(U1-PadAA1) -> Net-(U1-PadAA1)
- U1 pad AA2: unconnected-(U1-PadAA2) -> Net-(U1-PadAA2)
- U1 pad AA3: unconnected-(U1-PadAA3) -> Net-(U1-PadAA3)
- U1 pad AD3: unconnected-(U1-PadAD3) -> /QSGMII PHY/VSC_CLKOUT_1
- U1 pad AE2: unconnected-(U1-PadAE2) -> /QSGMII PHY/VSC_CLKOUT_0
- U1 pad AE22: unconnected-(U1-PadAE22) -> Net-(U1-PadAE22)
- U1 pad AF22: unconnected-(U1-PadAF22) -> Net-(U1-PadAF22)
- U1 pad AF3: unconnected-(U1-PadAF3) -> /QSGMII PHY/VSC_MDIO
- U1 pad AF4: unconnected-(U1-PadAF4) -> /QSGMII PHY/VSC_MDC
- U1 pad C12: unconnected-(U1-PadC12) -> /GND
- U1 pad C13: unconnected-(U1-PadC13) -> /GND
- U1 pad C14: unconnected-(U1-PadC14) -> /GND
- U1 pad C18: unconnected-(U1-PadC18) -> /2V5
- U1 pad C22: unconnected-(U1-PadC22) -> /GND
- U1 pad C23: unconnected-(U1-PadC23) -> /GND
- U1 pad C3: unconnected-(U1-PadC3) -> /QSGMII PHY/VSC_POWERDOWN
- U1 pad C4: unconnected-(U1-PadC4) -> /QSGMII PHY/VSC_RST_N
- U1 pad C7: unconnected-(U1-PadC7) -> /GND
- U1 pad C8: unconnected-(U1-PadC8) -> /GND
- U1 pad D17: unconnected-(U1-PadD17) -> /QSGMII PHY/VSC_JTAG_TCK
- U1 pad D18: unconnected-(U1-PadD18) -> /QSGMII PHY/VSC_JTAG_TDI
- U1 pad D19: unconnected-(U1-PadD19) -> /QSGMII PHY/VSC_JTAG_TDO
- U1 pad D20: unconnected-(U1-PadD20) -> /QSGMII PHY/VSC_JTAG_TMS
- U1 pad D21: unconnected-(U1-PadD21) -> Net-(U1-PadD21)
- U1 pad E13: unconnected-(U1-PadE13) -> Net-(U1-PadE13)
- U1 pad E14: unconnected-(U1-PadE14) -> Net-(U1-PadE14)
- U1 pad K23: unconnected-(U1-PadK23) -> Net-(U1-PadK23)
- U1 pad K4: unconnected-(U1-PadK4) -> Net-(U1-PadK4)
- U1 pad L23: unconnected-(U1-PadL23) -> Net-(U1-PadL23)
- U1 pad L4: unconnected-(U1-PadL4) -> Net-(U1-PadL4)
- U1 pad R1: unconnected-(U1-PadR1) -> /QSGMII PHY/VSC_FAST_STATUS
- U1 pad R2: unconnected-(U1-PadR2) -> /QSGMII PHY/VSC_MDINT
- U1 pad R4: unconnected-(U1-PadR4) -> Net-(U1-PadR4)
- U1 pad T1: unconnected-(U1-PadT1) -> Net-(U1-PadT1)
- U1 pad T2: unconnected-(U1-PadT2) -> Net-(U1-PadT2)
- U1 pad T3: unconnected-(U1-PadT3) -> Net-(U1-PadT3)
- U1 pad T4: unconnected-(U1-PadT4) -> Net-(U1-PadT4)
- U1 pad U1: unconnected-(U1-PadU1) -> Net-(U1-PadU1)
- U1 pad U2: unconnected-(U1-PadU2) -> Net-(U1-PadU2)
- U1 pad U3: unconnected-(U1-PadU3) -> Net-(U1-PadU3)
- U1 pad U4: unconnected-(U1-PadU4) -> Net-(U1-PadU4)
- U1 pad V1: unconnected-(U1-PadV1) -> Net-(U1-PadV1)
- U1 pad V2: unconnected-(U1-PadV2) -> Net-(U1-PadV2)
- U1 pad V3: unconnected-(U1-PadV3) -> Net-(U1-PadV3)
- U1 pad V4: unconnected-(U1-PadV4) -> Net-(U1-PadV4)
- U1 pad W1: unconnected-(U1-PadW1) -> Net-(U1-PadW1)
- U1 pad W2: unconnected-(U1-PadW2) -> Net-(U1-PadW2)
- U1 pad W3: unconnected-(U1-PadW3) -> Net-(U1-PadW3)
- U1 pad W4: unconnected-(U1-PadW4) -> Net-(U1-PadW4)
- U1 pad Y1: unconnected-(U1-PadY1) -> Net-(U1-PadY1)
- U1 pad Y2: unconnected-(U1-PadY2) -> Net-(U1-PadY2)
- U1 pad Y3: unconnected-(U1-PadY3) -> Net-(U1-PadY3)
- U1 pad Y4: unconnected-(U1-PadY4) -> Net-(U1-PadY4)
- U4 pad B12: unconnected-(U4-PadB12) -> /QSGMII PHY/VSC_POWERDOWN
- U4 pad D12: unconnected-(U4-PadD12) -> /QSGMII PHY/VSC_RST_N
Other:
- board size 145 x 134 mm -> 145 x 139 mm
